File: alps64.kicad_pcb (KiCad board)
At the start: 2 copper layers, 285 x 95 mm, 72 parts, among them K00 KEYSW, K01 KEYSW, K02 KEYSW, K03 KEYSW, K04 KEYSW, K05 KEYSW, K06 KEYSW, K07 KEYSW, K10_2 KEYSW, K11 KEYSW, K12 KEYSW, K13 KEYSW, K14 KEYSW, K15 KEYSW, K16 KEYSW, K17 KEYSW, K20 KEYSW, K21 KEYSW, K23 KEYSW, K24 KEYSW, K25 KEYSW, K27_1 KEYSW, K30 KEYSW, K31 KEYSW, K32 KEYSW, K33 KEYSW, K34 KEYSW, K35 KEYSW, K36 KEYSW, K37 KEYSW, K40 KEYSW, K42 KEYSW, K43 KEYSW, K44 KEYSW, K45 KEYSW, K46 KEYSW, K47 KEYSW, K50 KEYSW, K51 KEYSW, K52 KEYSW, K53 KEYSW, K54 KEYSW, K55 KEYSW, K56 KEYSW, K57 KEYSW, K60 KEYSW, K61 KEYSW, K62 KEYSW, K63 KEYSW, K64 KEYSW, K65 KEYSW, K66 KEYSW, K67 KEYSW, K71 KEYSW, K72 KEYSW, K73 KEYSW, K74 KEYSW, K75 KEYSW, K76 KEYSW, K77 KEYSW, P1 CONN_01X01

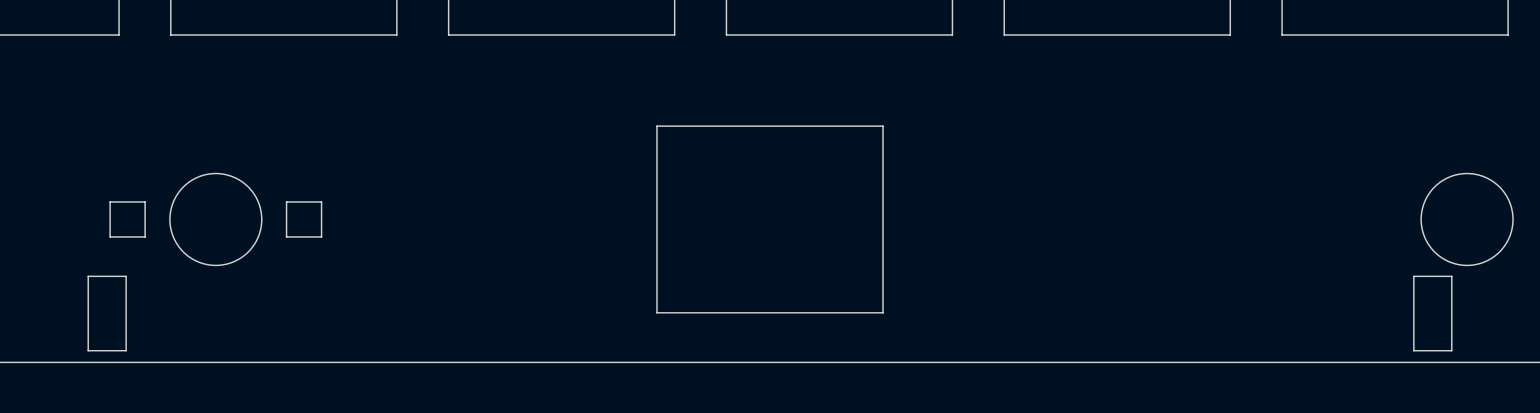
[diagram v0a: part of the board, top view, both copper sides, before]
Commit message: Add space bar flip support
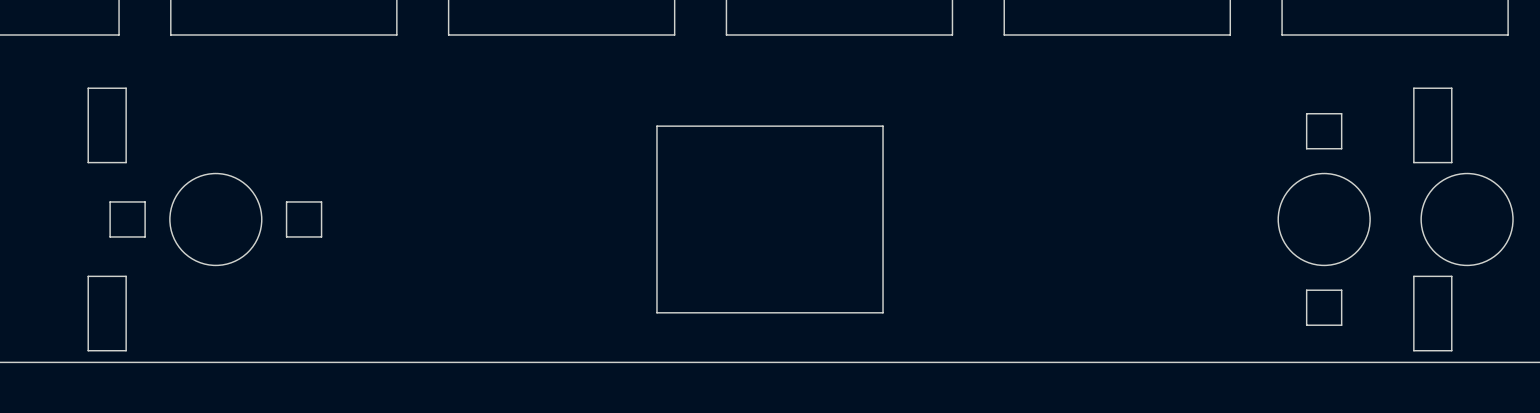
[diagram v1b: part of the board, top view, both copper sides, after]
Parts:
- added K60: KEYSW, keyboard_parts:ALPS_SKCM_CUTOUT_STAB883_flip, F.Cu at (147.6, 90.5)
- moved G*** 3.88 mm to (169.6, 88.0)
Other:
- board text added: "Ver.B_flip 2018/04"
